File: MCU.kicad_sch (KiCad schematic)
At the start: 48 parts, among them J1 JTAG, J2 HH-16P-CB-TYPE-C, J3 GPS, J4 CAM, J5 GPS, J6 CAM, Q1 SI2301BDS, SW1 TS2306A, SW2 TS2306A, U4 RP2354B, U5 W25Q128JVPIQ, U6 USBLC6-2P6, Y1 40MHz

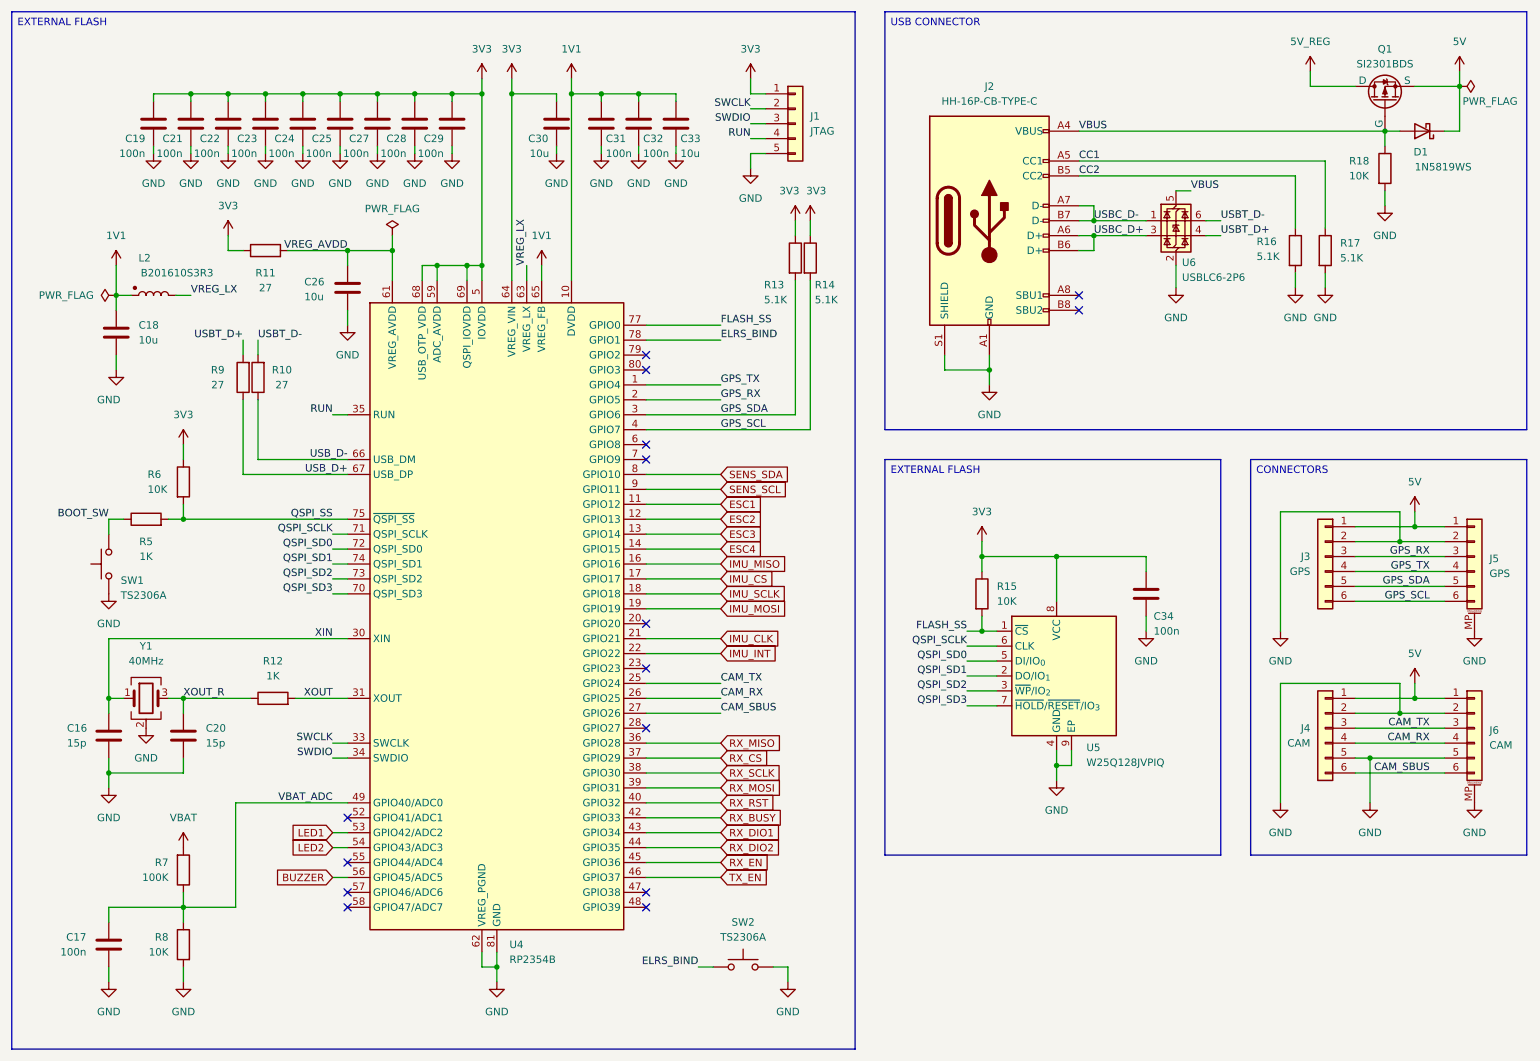
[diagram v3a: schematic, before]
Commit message: Initial layout
Completed an initial layout of the main components.

TODO
Route the ESCs and check the result.
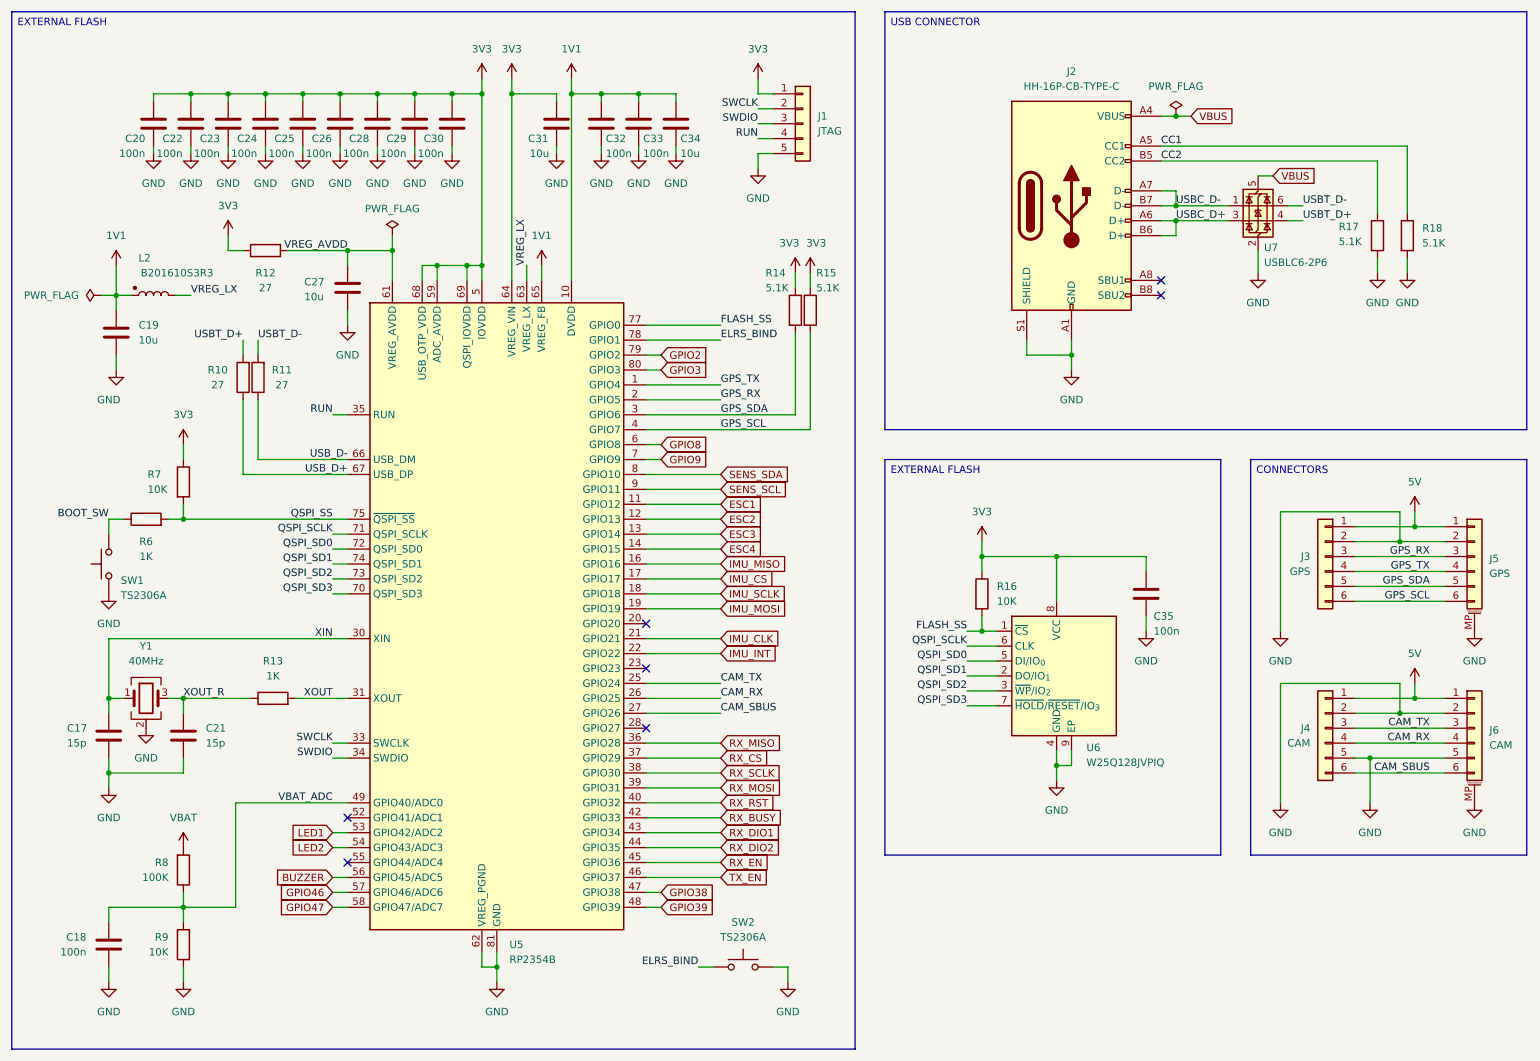
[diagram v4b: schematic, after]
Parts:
- removed D1: 1N5819WS, Diode_SMD:D_SOD-323, symbol Diode:1N5819WS
- removed Q1: SI2301BDS, Package_TO_SOT_SMD:SOT-23, symbol Custom_Parts:SI2301BDS
- removed R18: 10K, Resistor_SMD:R_0603_1608Metric, symbol Device:R
- C19: renamed from C18; footprint Capacitor_SMD:C_0805_2012Metric -> Capacitor_SMD:C_0603_1608Metric
- C27: renamed from C26; footprint Capacitor_SMD:C_0805_2012Metric -> Capacitor_SMD:C_0603_1608Metric
- C31: renamed from C30; footprint Capacitor_SMD:C_0805_2012Metric -> Capacitor_SMD:C_0603_1608Metric
- C34: renamed from C33; footprint Capacitor_SMD:C_0805_2012Metric -> Capacitor_SMD:C_0603_1608Metric
- renumbered C16 to C17, C17 to C18, C19 to C20, C20 to C21, C21 to C22, C22 to C23, C23 to C24, C24 to C25, C25 to C26, C27 to C28, C28 to C29, C29 to C30, C31 to C32, C32 to C33, C34 to C35, R9 to R10, R10 to R11, R11 to R12, R12 to R13, R13 to R14, R14 to R15, R15 to R16, R16 to R17, R17 to R18, R5 to R6, R6 to R7, R7 to R8, R8 to R9, U4 to U5, U5 to U6, U6 to U7
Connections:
- net GPIO38: now reaches U5.47 (GPIO38)
- net GPIO39: now reaches U5.48 (GPIO39)
- net GPIO46: now reaches U5.57 (GPIO46/ADC6)
- net GPIO47: now reaches U5.58 (GPIO47/ADC7)
- net GPIO8: now reaches U5.6 (GPIO8)
- net GPIO9: now reaches U5.7 (GPIO9)
- net GPIO2: now reaches U5.79 (GPIO2)
- net GPIO3: now reaches U5.80 (GPIO3)
- no-connect marks 15 -> 7
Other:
- moved on the sheet: J1, J2, R14, R15, R17, R18, U7

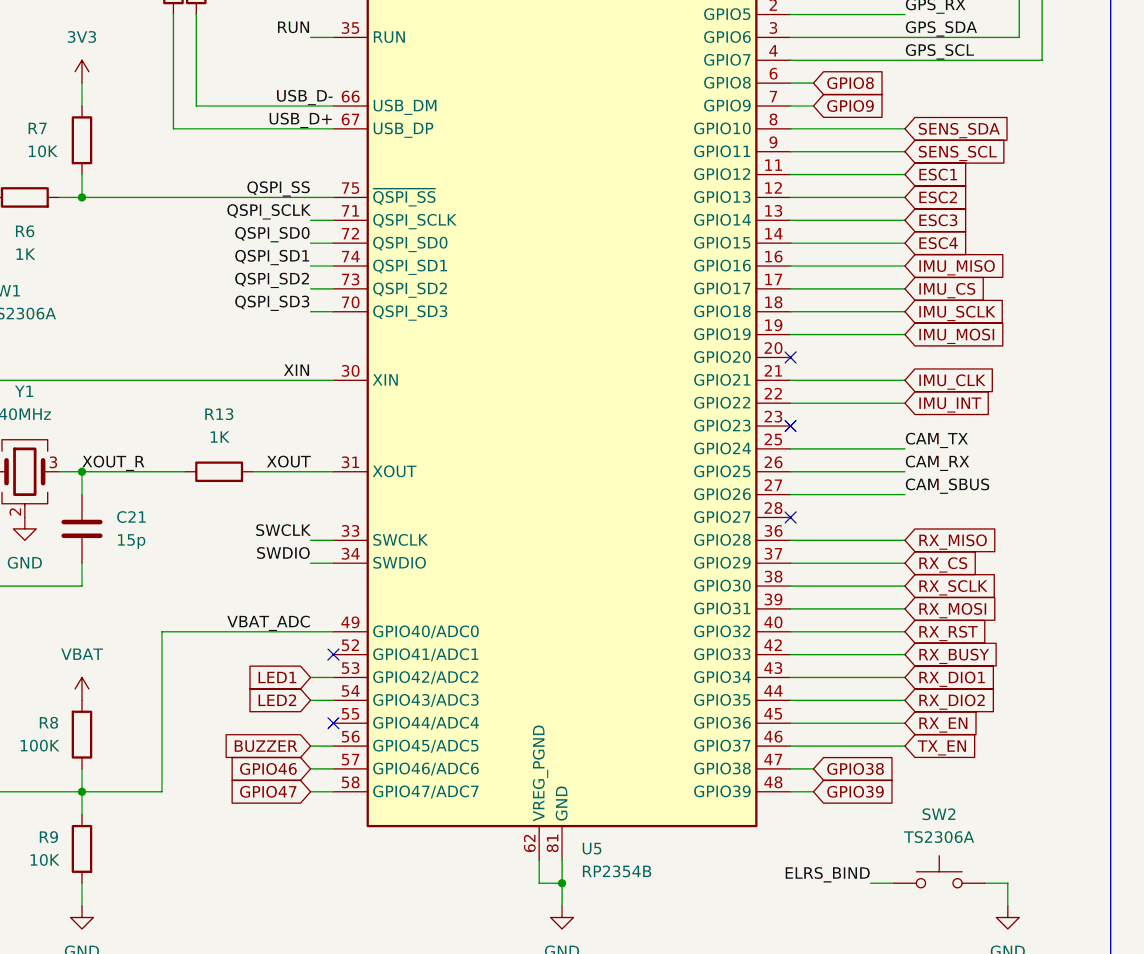
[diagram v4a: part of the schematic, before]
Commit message: MCU layout
Updated the schematic labels.
Continued the MCU layout.
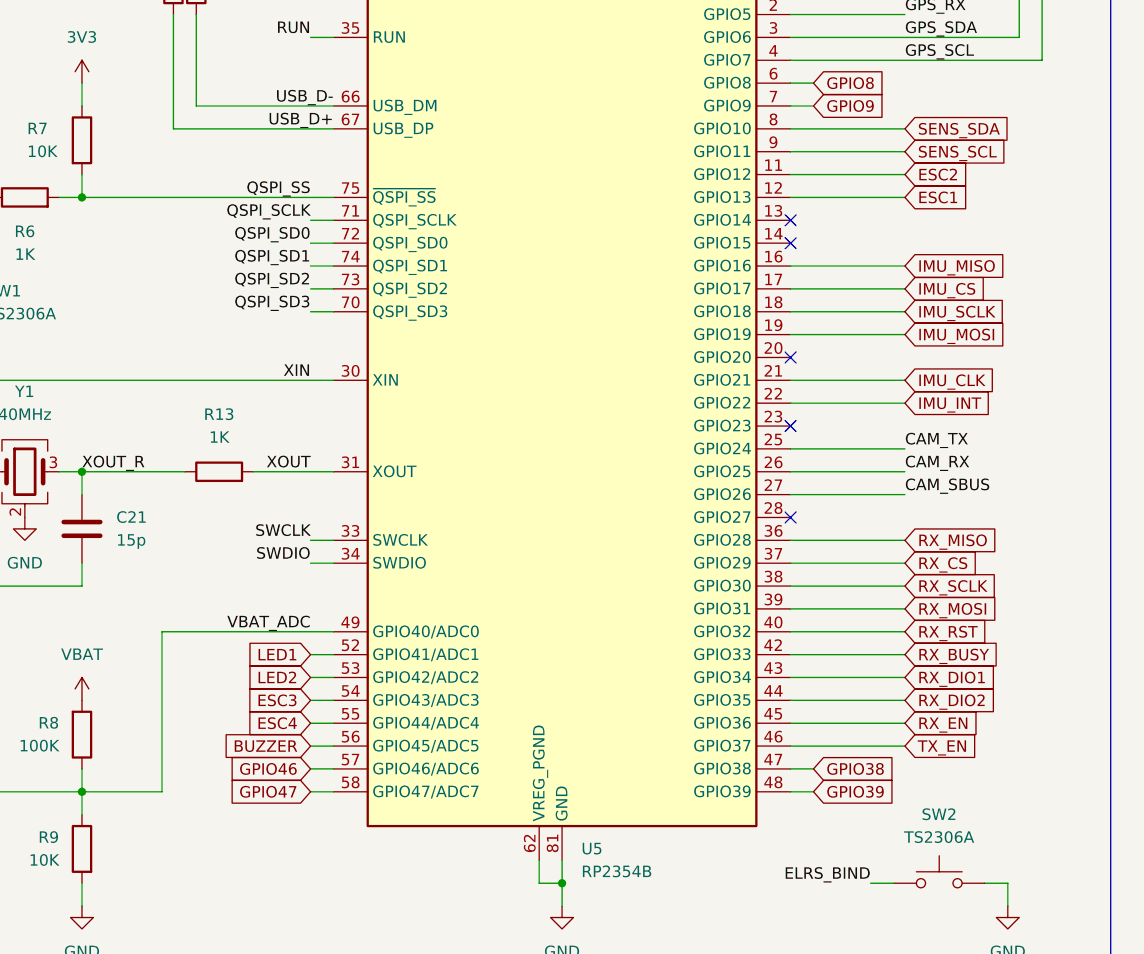
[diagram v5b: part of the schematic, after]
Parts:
- C35: footprint Capacitor_SMD:C_0805_2012Metric -> Capacitor_SMD:C_0603_1608Metric
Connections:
- net ESC1: now also U5.12 (GPIO13); no longer U5.11 (GPIO12)
- net ESC2: now also U5.11 (GPIO12); no longer U5.12 (GPIO13)
- net ESC3: now also U5.54 (GPIO43/ADC3); no longer U5.13 (GPIO14)
- net ESC4: now also U5.55 (GPIO44/ADC4); no longer U5.14 (GPIO15)
- net LED1: now also U5.52 (GPIO41/ADC1); no longer U5.53 (GPIO42/ADC2)
- net LED2: now also U5.53 (GPIO42/ADC2); no longer U5.54 (GPIO43/ADC3)

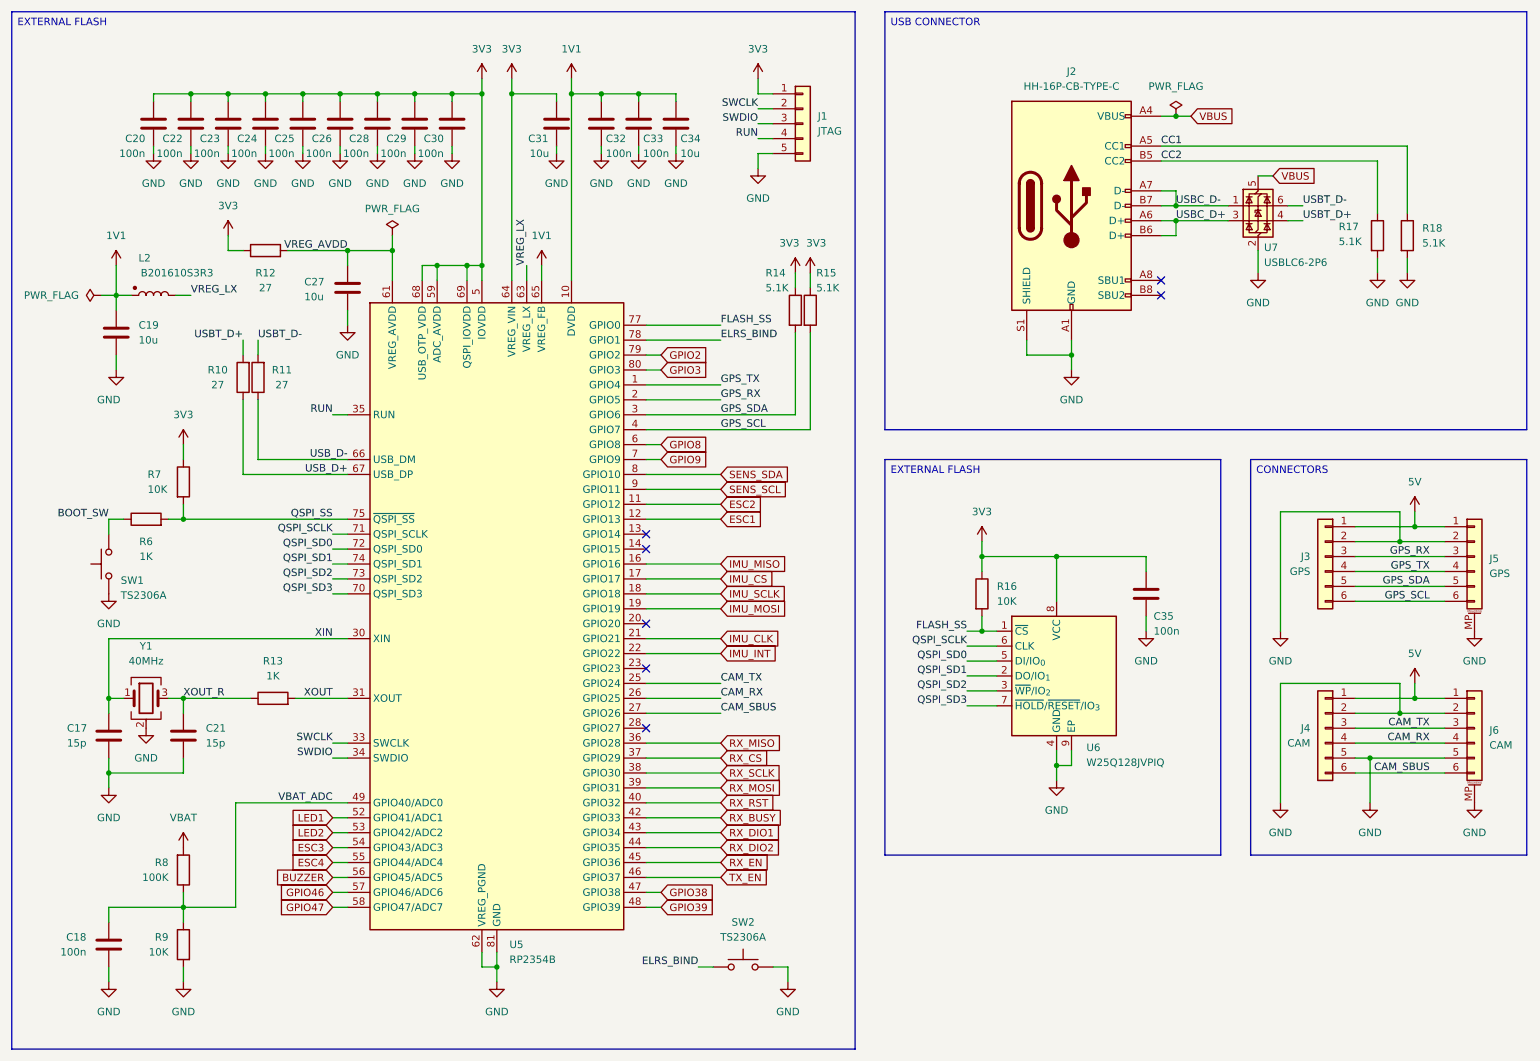
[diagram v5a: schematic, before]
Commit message: Schematic revision
Added an ESP32 C3 for the ELRS receiver.
Updated the protection approach for the board.
Updated the net nodes.
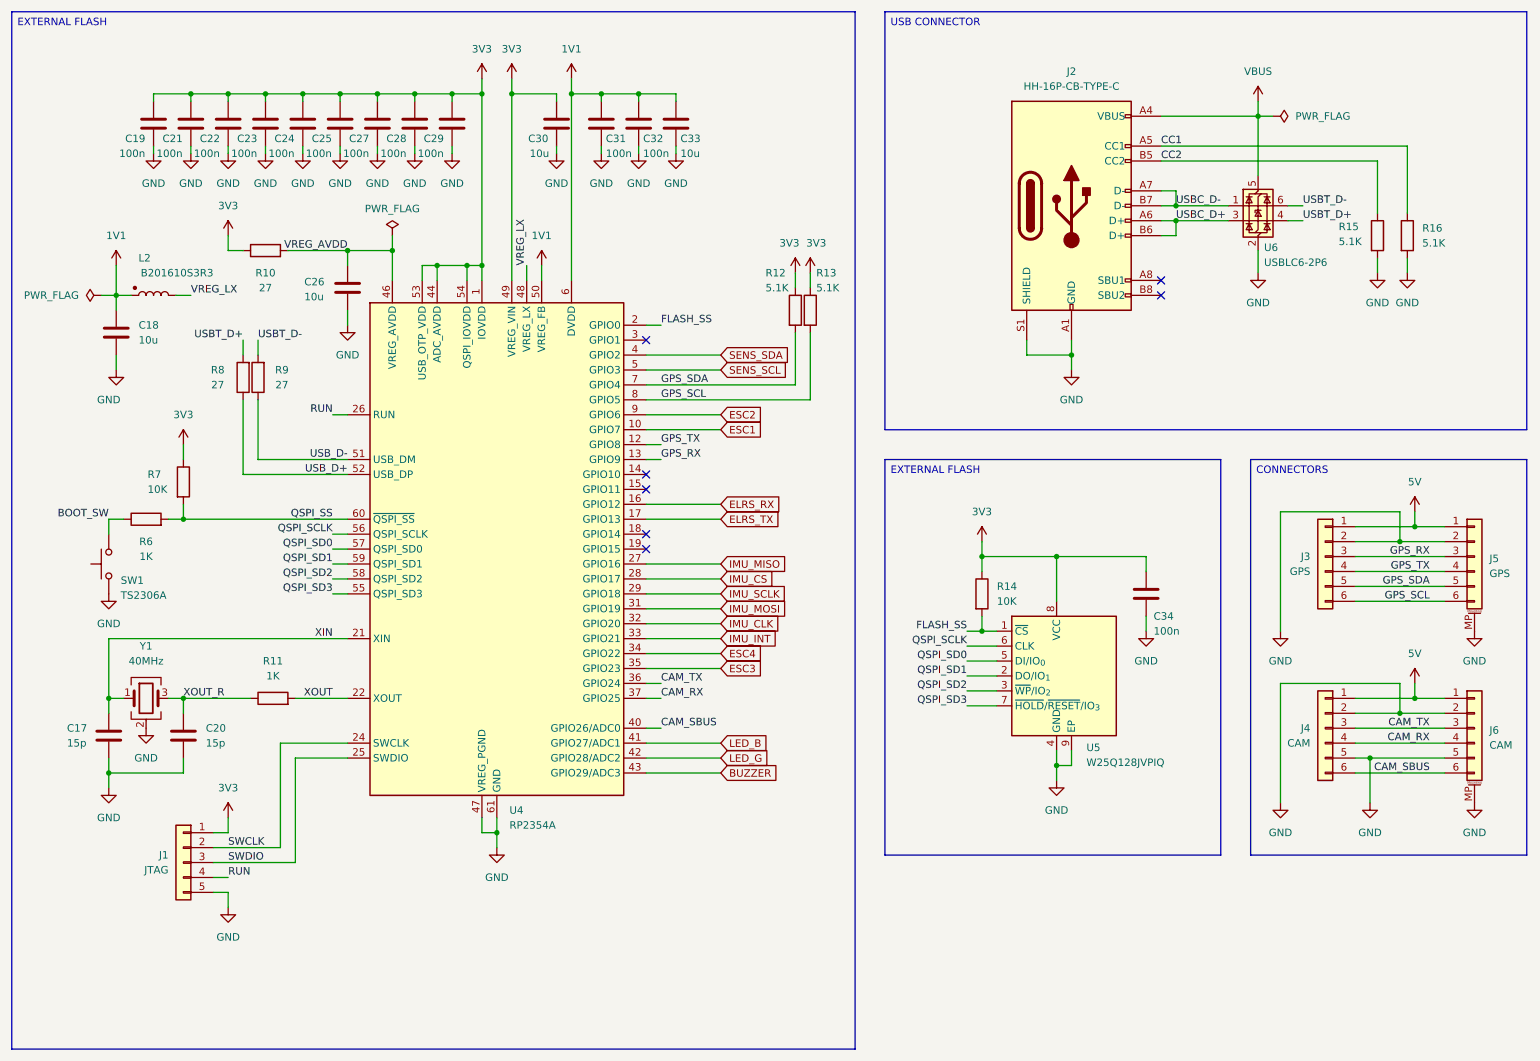
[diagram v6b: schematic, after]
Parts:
- removed C18: 100n, Capacitor_SMD:C_0603_1608Metric, symbol Device:C
- removed R8: 100K, Resistor_SMD:R_0603_1608Metric, symbol Device:R
- removed R9: 10K, Resistor_SMD:R_0603_1608Metric, symbol Device:R
- removed SW2: TS2306A, Custom_Parts:SW_SMD_3.0x2.0_PUSH, symbol Switch:SW_Push
- removed U5: RP2354B, Custom_Parts:RP2350B_QFN-80_EP_10.573x10.573_Pitch0.4mm, symbol MCU_RaspberryPi:RP2354B
- added U4: RP2354A, Custom_Parts:RP2350A_QFN-60_EP_7.75x7.75_Pitch0.4mm, symbol MCU_RaspberryPi:RP2354A
- renumbered C19 to C18, C20 to C19, C21 to C20, C22 to C21, C23 to C22, C24 to C23, C25 to C24, C26 to C25, C27 to C26, C28 to C27, C29 to C28, C30 to C29, C31 to C30, C32 to C31, C33 to C32, C34 to C33, C35 to C34, R12 to R10, R13 to R11, R14 to R12, R15 to R13, R16 to R14, R17 to R15, R18 to R16, R10 to R8, R11 to R9, U6 to U5, U7 to U6
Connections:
- net 1V1: now also U4.23 (DVDD), U4.39 (DVDD), U4.50 (VREG_FB), U4.6 (DVDD)
- net 3V3: now also U4.1 (IOVDD), U4.11 (IOVDD), U4.20 (IOVDD), U4.30 (IOVDD), U4.38 (IOVDD), U4.44 (ADC_AVDD), U4.45 (IOVDD), U4.49 (VREG_VIN), U4.53 (USB_OTP_VDD), U4.54 (QSPI_IOVDD)
- net BUZZER: now also U4.43 (GPIO29/ADC3)
- net CAM_RX: now also U4.37 (GPIO25)
- net CAM_SBUS: now also U4.40 (GPIO26/ADC0)
- net CAM_TX: now also U4.36 (GPIO24)
- net ESC1: now also U4.10 (GPIO7)
- net ESC2: now also U4.9 (GPIO6)
- net ESC3: now also U4.35 (GPIO23)
- net ESC4: now also U4.34 (GPIO22)
- net FLASH_SS: now also U4.2 (GPIO0)
- net GND: now also U4.47 (VREG_PGND), U4.61 (GND)
- net GPS_RX: now also U4.13 (GPIO9)
- net GPS_SCL: now also U4.8 (GPIO5)
- net GPS_SDA: now also U4.7 (GPIO4)
- net GPS_TX: now also U4.12 (GPIO8)
- net IMU_CLK: now also U4.32 (GPIO20)
- net IMU_CS: now also U4.28 (GPIO17)
- net IMU_INT: now also U4.33 (GPIO21)
- net IMU_MISO: now also U4.27 (GPIO16)
- net IMU_MOSI: now also U4.31 (GPIO19)
- net IMU_SCLK: now also U4.29 (GPIO18)
- net QSPI_SCLK: now also U4.56 (QSPI_SCLK)
- net QSPI_SD0: now also U4.57 (QSPI_SD0)
- net QSPI_SD1: now also U4.59 (QSPI_SD1)
- net QSPI_SD2: now also U4.58 (QSPI_SD2)
- net QSPI_SD3: now also U4.55 (QSPI_SD3)
- net QSPI_SS: now also U4.60 (~{QSPI_SS})
- net RUN: now also U4.26 (RUN)
- net SENS_SCL: now also U4.5 (GPIO3)
- net SENS_SDA: now also U4.4 (GPIO2)
- net SWCLK: now also U4.24 (SWCLK)
- net SWDIO: now also U4.25 (SWDIO)
- net USB_D+: now also U4.52 (USB_DP)
- net USB_D-: now also U4.51 (USB_DM)
- net VREG_AVDD: now also U4.46 (VREG_AVDD)
- net VREG_LX: now also U4.48 (VREG_LX)
- net XIN: now also U4.21 (XIN)
- net XOUT: now also U4.22 (XOUT)
- new net ELRS_RX: U4.16 (GPIO12)
- new net ELRS_TX: U4.17 (GPIO13)
- new net LED_B: U4.41 (GPIO27/ADC1)
- new net LED_G: U4.42 (GPIO28/ADC2)
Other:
- moved on the sheet: J1
